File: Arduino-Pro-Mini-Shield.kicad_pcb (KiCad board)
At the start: 2 copper layers, 38 x 44 mm, 12 parts, among them CON1 AVR-ISP-6, IC1 ArduinoProMini, J1 Conn_01x03, J2 Conn_02x09_Odd_Even, J3 Conn_01x03, J4 Conn_02x04_Odd_Even

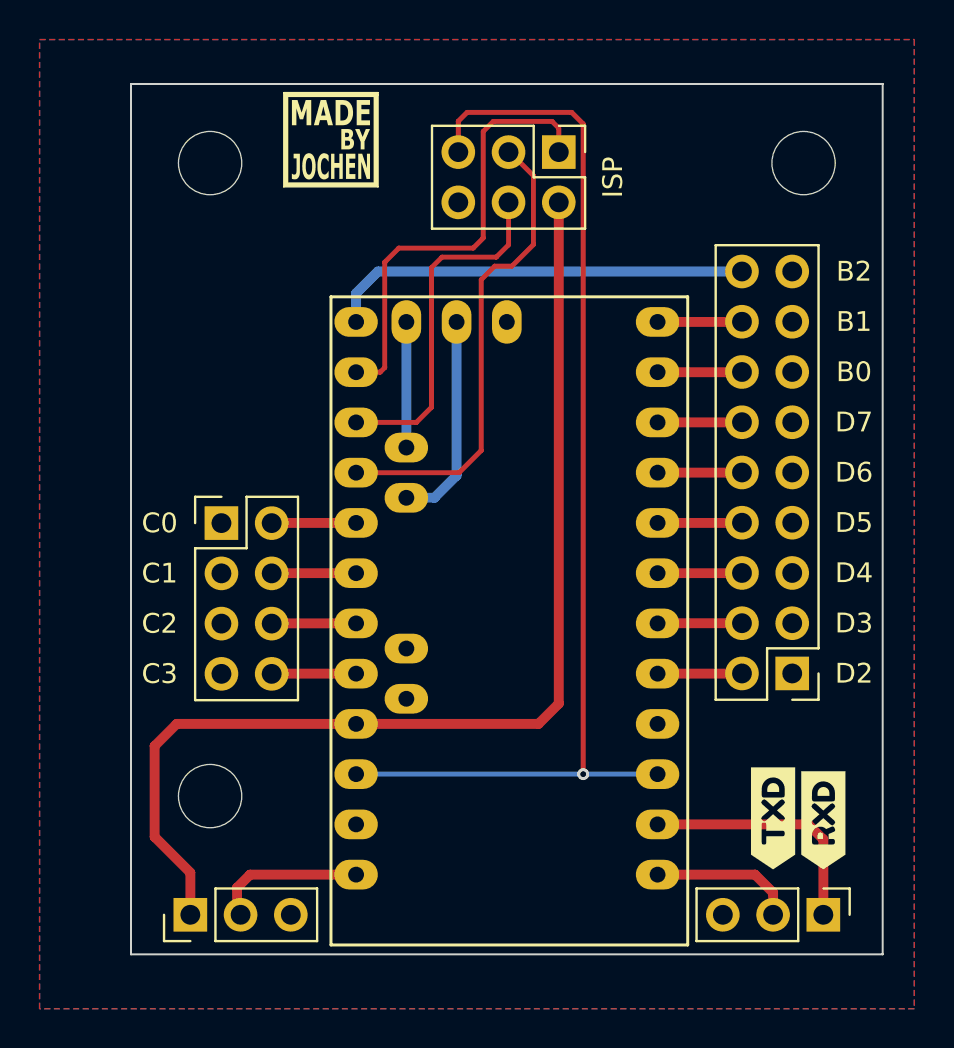
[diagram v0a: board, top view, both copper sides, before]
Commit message: BUGFIX: swapped MOSI and MISO
added also pins for SPI and I2C
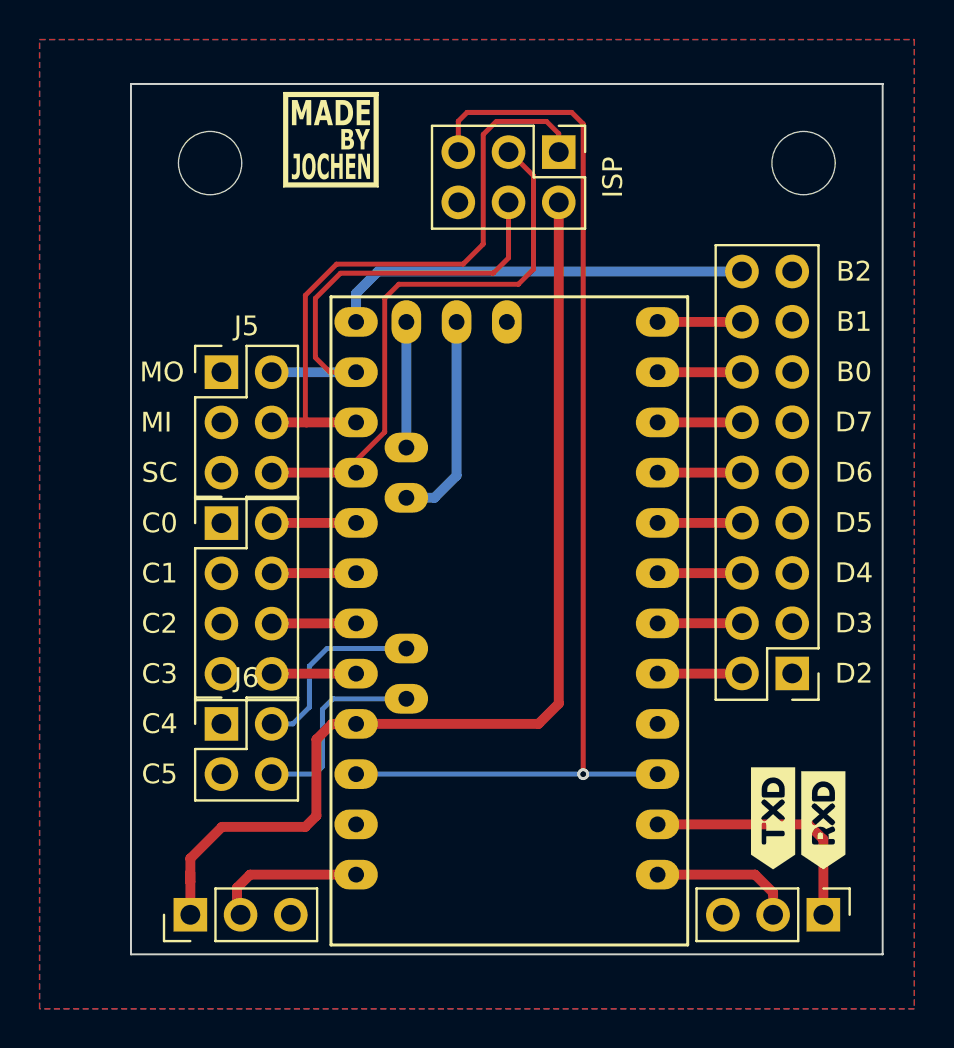
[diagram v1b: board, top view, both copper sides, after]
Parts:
- removed H2: MountingHole, MountingHole:MountingHole_3.2mm_M3
- added J5: Conn_02x03_Odd_Even, Connector_PinHeader_2.54mm:PinHeader_2x03_P2.54mm_Vertical, F.Cu at (101.2, 75.6)
- added J6: Conn_02x02_Odd_Even, Connector_PinHeader_2.54mm:PinHeader_2x02_P2.54mm_Vertical, F.Cu at (101.2, 93.4)
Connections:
- CON1 pad 1: /MOSI -> /MISO
- CON1 pad 4: /MISO -> /MOSI
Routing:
- net /MISO: track 17.7 -> 31.6 mm
- net /C5: track 0.00 -> 10.1 mm
- net /C4: track 0.00 -> 9.61 mm
- net /SCK: track 24.0 -> 28.2 mm
- net VCC: track 55.9 -> 52.8 mm
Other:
- board text added: "C4"
- board text added: "C5"
- board text added: "MI"
- board text added: "MO"
- board text added: "SC"

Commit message: slightly adjusted silkscreen
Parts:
- moved G*** 38.0 mm to (115.6, 100.9)
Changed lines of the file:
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@@
     (property "Sheetname" "")
     (attr through_hole)
-    (fp_text reference "J5" (at 1.27 -2.33) (layer "F.SilkS")
+    (fp_text reference "J5" (at 1.27 -2.33) (layer "F.SilkS") hide
       (effects (font (size 1 1) (thickness 0.15)))
     )
@@
     (property "Sheetname" "")
     (attr through_hole)
-    (fp_text reference "J6" (at 1.27 -2.33) (layer "F.SilkS")
+    (fp_text reference "J6" (at 1.27 -2.33) (layer "F.SilkS") hide
       (effects (font (size 1 1) (thickness 0.15)))
     )
@@
   )
   (footprint "MadeByJochen:MadeByJochen_5x5" (layer "F.Cu")
-    (at 106.7816 63.9318)
+    (at 115.648911 100.853633)
     (attr board_only exclude_from_pos_files exclude_from_bom)
     (fp_text reference "G***" (at -2.4 -3.5) (layer "F.SilkS") hide
@@
     )
   )
+  (gr_rect (start 114.8588 62.738) (end 116.586 63.1444) (layer "F.SilkS") (width 0.15) (fill solid))
   (gr_line (start 96.6462 61.0458) (end 134.6462 61.0458) (layer "Edge.Cuts") (width 0.1))
   (gr_line (start 96.6462 105.0458) (end 96.6462 61.0458) (layer "Edge.Cuts") (width 0.1))
